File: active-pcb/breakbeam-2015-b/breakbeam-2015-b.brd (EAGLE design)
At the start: 10.8 x 16.5 mm, 5 parts, among them J1 1814650

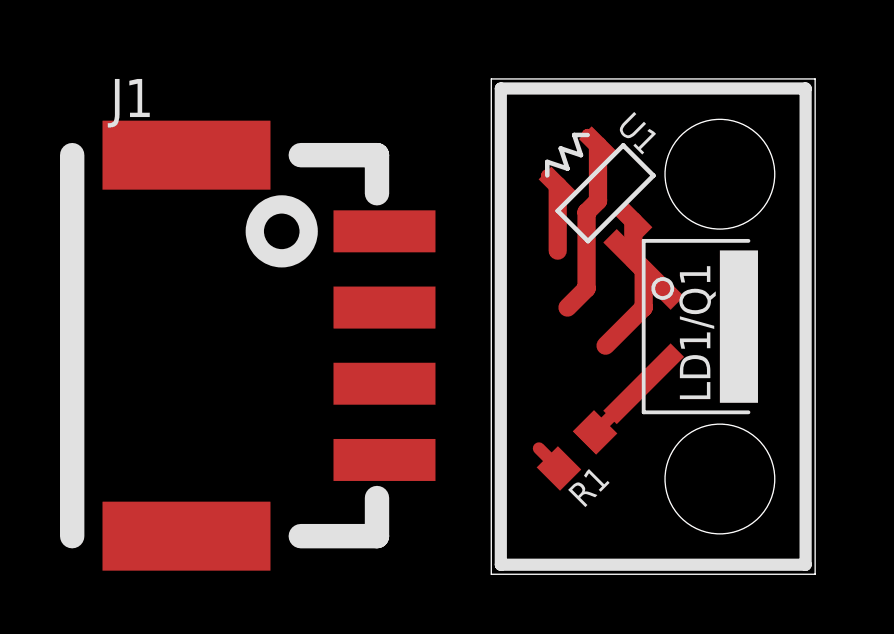
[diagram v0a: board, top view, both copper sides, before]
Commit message: preliminary Breakbeam revB design
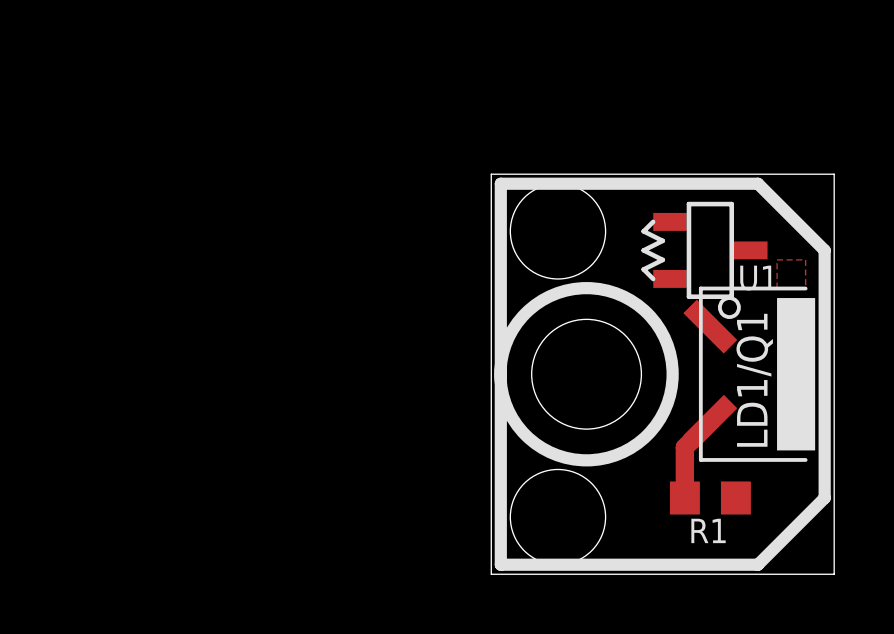
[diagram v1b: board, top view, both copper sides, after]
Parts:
- removed J1: 1814650, RoboJackets-Connectors:1814650
- LD1/Q1: device RoboJackets-Diodes:2LEAD_H_FACEDOWN_SHORT_MIN -> RoboJackets-Diodes:2LEAD_H_FACEDOWN_XSHORT_MIN
- moved R1 4.72 mm to (7.30, 2.54), turned to 180 degrees
- moved R3 4.27 mm to (5.40, 10.8), turned to 270 degrees
- moved U1 3.98 mm to (7.30, 10.8), turned to 90 degrees
- moved LD1/Q1 2.48 mm to (7.62, 6.67)
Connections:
- net +5V: no longer J1.1
- net GND: no longer J1.3
- net OPTICAL: no longer J1.4
- net SERIAL_ID: no longer J1.2
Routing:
- net SERIAL_ID: track 6.32 -> 0.00 mm
- net GND: track 4.83 -> 0.00 mm
- net +5V: track 2.66 -> 0.00 mm
- net OPTICAL: track 0.95 -> 0.00 mm
- added copper zone on layer 1, net GND
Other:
- board size 10.8 x 16.5 mm -> 11.4 x 13.3 mm
- board text added: "RJRC-SSL Breakbeam/ID"
- board text removed: "RoboJackets RoboCup Breakbeam/ID"
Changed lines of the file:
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@@
 <setting verticaltext="up"/>
 </settings>
-<grid distance="0.025" unitdist="inch" unit="inch" style="lines" multiple="1" display="yes" altdistance="0.0125" altunitdist="inch" altunit="inch"/>
+<grid distance="0.0125" unitdist="inch" unit="inch" style="lines" multiple="1" display="yes" altdistance="0.0125" altunitdist="inch" altunit="inch"/>
 <layers>
 <layer number="1" name="Top" color="4" fill="1" visible="yes" active="yes"/>
@@
 <layer number="20" name="Dimension" color="15" fill="1" visible="yes" active="yes"/>
 <layer number="21" name="tPlace" color="7" fill="1" visible="yes" active="yes"/>
-<layer number="22" name="bPlace" color="7" fill="1" visible="yes" active="yes"/>
+<layer number="22" name="bPlace" color="7" fill="1" visible="no" active="yes"/>
 <layer number="23" name="tOrigins" color="15" fill="1" visible="yes" active="yes"/>
 <layer number="24" name="bOrigins" color="15" fill="1" visible="yes" active="yes"/>
@@
 <board>
 <plain>
-<wire x1="0" y1="0" x2="10.795" y2="0" width="0" layer="20"/>
-<wire x1="10.795" y1="0" x2="10.795" y2="16.51" width="0" layer="20"/>
-<wire x1="10.795" y1="16.51" x2="0" y2="16.51" width="0" layer="20"/>
-<wire x1="0" y1="16.51" x2="0" y2="0" width="0" layer="20"/>
-<hole x="7.62" y="3.175" drill="3.6576"/>
-<hole x="7.62" y="13.335" drill="3.6576"/>
-<text x="4.445" y="13.97" size="1.016" layer="22" rot="MR270">RoboJackets
-RoboCup
+<wire x1="0" y1="0" x2="11.43" y2="0" width="0" layer="20"/>
+<wire x1="11.43" y1="0" x2="11.43" y2="13.335" width="0" layer="20"/>
+<wire x1="11.43" y1="13.335" x2="0" y2="13.335" width="0" layer="20"/>
+<wire x1="0" y1="13.335" x2="0" y2="0" width="0" layer="20"/>
+<hole x="3.175" y="6.6675" drill="3.6576"/>
+<text x="7.9375" y="11.1125" size="1.016" layer="22" rot="MR270">RJRC-SSL
 Breakbeam/ID</text>
-<rectangle x1="4.445" y1="6.35" x2="8.255" y2="10.16" layer="22"/>
-<wire x1="0.3175" y1="16.1925" x2="10.4775" y2="16.1925" width="0.4064" layer="21"/>
-<wire x1="10.4775" y1="16.1925" x2="10.4775" y2="0.3175" width="0.4064" layer="21"/>
-<wire x1="10.4775" y1="0.3175" x2="0.3175" y2="0.3175" width="0.4064" layer="21"/>
-<wire x1="0.3175" y1="0.3175" x2="0.3175" y2="16.1925" width="0.4064" layer="21"/>
+<wire x1="0.3175" y1="13.0175" x2="8.89" y2="13.0175" width="0.4064" layer="21"/>
+<wire x1="8.89" y1="13.0175" x2="11.1125" y2="10.795" width="0.4064" layer="21"/>
+<wire x1="11.1125" y1="10.795" x2="11.1125" y2="2.54" width="0.4064" layer="21"/>
+<wire x1="11.1125" y1="2.54" x2="8.89" y2="0.3175" width="0.4064" layer="21"/>
+<wire x1="8.89" y1="0.3175" x2="0.3175" y2="0.3175" width="0.4064" layer="21"/>
+<wire x1="0.3175" y1="0.3175" x2="0.3175" y2="13.0175" width="0.4064" layer="21"/>
+<circle x="3.175" y="6.6675" radius="2.8702" width="0.4064" layer="21"/>
+<hole x="2.2225" y="1.905" drill="3.175"/>
+<hole x="2.2225" y="11.43" drill="3.175"/>
 </plain>
 <attributes>
@@
 </autorouter>
 <elements>
-<element name="LD1/Q1" library="RoboJackets-Diodes" package="2LEAD_H_FACEDOWN_SHORT_MIN" value="" x="5.715" y="8.255" smashed="yes">
-<attribute name="NAME" x="7.3025" y="5.715" size="1.016" layer="21" rot="R90"/>
+<element name="LD1/Q1" library="RoboJackets-Diodes" package="2LEAD_H_FACEDOWN_XSHORT_MIN" value="" x="7.62" y="6.6675" smashed="yes">
+<attribute name="NAME" x="9.2075" y="4.1275" size="1.016" layer="21" rot="R90"/>
 </element>
-<element name="R1" library="rcl" package="R0603" value="" x="2.8575" y="4.1275" smashed="yes" rot="R45">
-<attribute name="NAME" x="3.06605" y="2.168025" size="0.8128" layer="25" rot="R45"/>
+<element name="R1" library="rcl" package="R0603" value="" x="7.3025" y="2.54" smashed="yes" rot="R180">
+<attribute name="NAME" x="7.90559375" y="1.850528125" size="0.8128" layer="25" rot="R180"/>
 </element>
-<element name="U1" library="RoboJackets-ICs" package="SOT-23-3" value="" x="3.81" y="12.7" smashed="yes" rot="R45">
-<attribute name="NAME" x="4.1275" y="14.896971875" size="0.8128" layer="25" ratio="10" rot="R315"/>
-<attribute name="VALUE" x="7.222496875" y="13.598025" size="1.27" layer="27" ratio="10" rot="R135"/>
+<element name="U1" library="RoboJackets-ICs" package="SOT-23-3" value="" x="7.3025" y="10.795" smashed="yes" rot="R90">
+<attribute name="NAME" x="9.583984375" y="10.287" size="0.8128" layer="25" ratio="10" rot="R180"/>
+<attribute name="VALUE" x="9.080503125" y="13.842996875" size="1.27" layer="27" ratio="10" rot="R180"/>
 </element>
-<element name="R3" library="RoboJackets-Resistors" package="GHOST_0.075" value="0.3k-2.2k" x="2.54" y="13.97" rot="R225"/>
-<element name="J1" library="RoboJackets-Connectors" package="1814650" value="1814650" x="-10.16" y="7.62" rot="R270"/>
+<element name="R3" library="RoboJackets-Resistors" package="GHOST_0.075" value="0.3k-2.2k" x="5.3975" y="10.795" rot="R270"/>
 </elements>
 <signals>
@@
 <contactref element="LD1/Q1" pad="2"/>
 <contactref element="R1" pad="2"/>
-<wire x1="5.715" y1="6.985" x2="5.08" y2="6.35" width="0.4064" layer="1"/>
-<wire x1="5.08" y1="6.35" x2="3.458540625" y2="4.728540625" width="0.4064" layer="1"/>
+<wire x1="6.4525" y1="2.54" x2="6.4525" y2="4.23" width="0.6096" layer="1"/>
+<wire x1="6.4525" y1="4.23" x2="7.3025" y2="5.08" width="0.6096" layer="1"/>
 </signal>
 <signal name="GND">
 <contactref element="LD1/Q1" pad="1"/>
 <contactref element="U1" pad="3"/>
-<wire x1="3.81" y1="7.62" x2="5.08" y2="8.89" width="0.6096" layer="1"/>
-<wire x1="5.08" y1="10.16" x2="5.08" y2="8.89" width="0.6096" layer="1"/>
-<wire x1="4.73348125" y1="11.776515625" x2="4.73348125" y2="10.50651875" width="0.6096" layer="1"/>
-<wire x1="4.73348125" y1="10.50651875" x2="5.08" y2="10.16" width="0.6096" layer="1"/>
-<contactref element="J1" pad="3"/>
-<wire x1="-3.56" y1="6.35" x2="3.81" y2="7.62" width="0" layer="19" extent="1-1"/>
+<polygon width="0.254" layer="1">
+<vertex x="9.525" y="10.4775"/>
+<vertex x="10.4775" y="10.4775"/>
+<vertex x="10.4775" y="9.525"/>
+<vertex x="9.525" y="9.525"/>
+</polygon>
+<wire x1="7.3025" y1="8.255" x2="8.6085" y2="10.795" width="0" layer="19" extent="1-1"/>
 </signal>
 <signal name="+5V">
 <contactref element="U1" pad="2"/>
 <contactref element="R3" pad="P$2"/>
-<wire x1="2.214765625" y1="12.951728125" x2="2.214765625" y2="10.787265625" width="0.6096" layer="1"/>
-<wire x1="1.866478125" y1="13.296478125" x2="1.870015625" y2="13.296478125" width="0.4064" layer="1"/>
-<wire x1="1.870015625" y1="13.296478125" x2="2.214765625" y2="12.951728125" width="0.4064" layer="1"/>
-<contactref element="J1" pad="1"/>
-<wire x1="-3.56" y1="11.43" x2="2.214765625" y2="10.787265625" width="0" layer="19" extent="1-1"/>
+<wire x1="5.3975" y1="9.8425" x2="5.9965" y2="9.845" width="0" layer="19" extent="1-1"/>
 </signal>
 <signal name="SERIAL_ID">
 <contactref element="U1" pad="1"/>
 <contactref element="R3" pad="P$1"/>
-<wire x1="2.54" y1="8.89" x2="3.175" y2="9.525" width="0.6096" layer="1"/>
-<wire x1="3.55826875" y1="14.29523125" x2="3.55826875" y2="12.44826875" width="0.6096" layer="1"/>
-<wire x1="3.55826875" y1="12.44826875" x2="3.175" y2="12.065" width="0.6096" layer="1"/>
-<wire x1="3.175" y1="12.065" x2="3.175" y2="9.525" width="0.6096" layer="1"/>
-<wire x1="3.21351875" y1="14.64351875" x2="3.21351875" y2="14.63998125" width="0.4064" layer="1"/>
-<wire x1="3.21351875" y1="14.63998125" x2="3.55826875" y2="14.29523125" width="0.4064" layer="1"/>
-<contactref element="J1" pad="2"/>
-<wire x1="-3.56" y1="8.89" x2="2.54" y2="8.89" width="0" layer="19" extent="1-1"/>
+<wire x1="5.3975" y1="11.7475" x2="5.9965" y2="11.745" width="0" layer="19" extent="1-1"/>
 </signal>
 <signal name="OPTICAL">
 <contactref element="R1" pad="1"/>
-<wire x1="1.5875" y1="4.1954125" x2="2.25645625" y2="3.52645625" width="0.4064" layer="1"/>
-<contactref element="J1" pad="4"/>
-<wire x1="2.25645625" y1="3.52645625" x2="-3.56" y2="3.81" width="0" layer="19" extent="1-1"/>
 </signal>
 </signals>

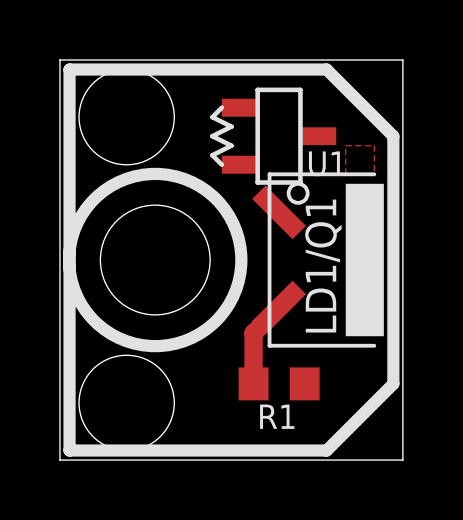
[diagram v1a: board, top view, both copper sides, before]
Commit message: Breakbeam revB update
added planes on top layer to maximize adhesion
added anchored support pads for diode tensioner (only use if necessary)
added offset plane near the mounting holes to make the bottom side level
(the bottom plane for the anchor will have a non-zero height)
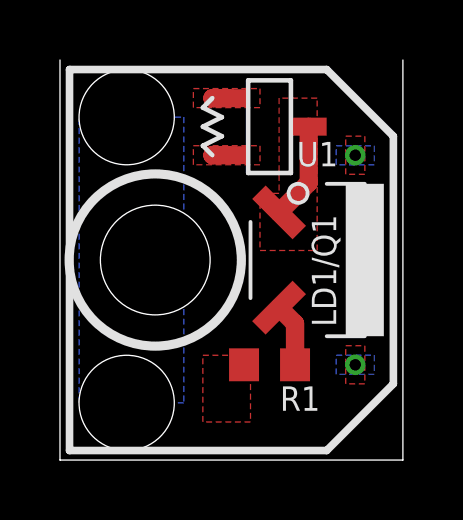
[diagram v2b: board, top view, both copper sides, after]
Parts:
- moved R1 0.71 mm to (6.99, 3.17), turned to 0 degrees
- moved R3 0.45 mm to (5.08, 11.1)
- moved U1 0.45 mm to (6.99, 11.1)
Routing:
- net GND: track 0.00 -> 3.27 mm
- net N$1: track 2.89 -> 2.13 mm
- net SERIAL_ID: track 0.00 -> 0.60 mm
- net +5V: track 0.00 -> 0.60 mm
- added copper zone on layer 1, net +5V
- added copper zone on layer 1, net FLOAT1
- added copper zone on layer 16, net FLOAT1
- added copper zone on layer 1, net FLOAT2
- added copper zone on layer 16, net FLOAT2
- added copper zone on layer 16, net FLOAT3
- added copper zone on layer 1, net OPTICAL
- added copper zone on layer 1, net SERIAL_ID
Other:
- board text added: "+5V"
- board text added: "GND"
- board text added: "ID"
- board text added: "OPTICAL"
